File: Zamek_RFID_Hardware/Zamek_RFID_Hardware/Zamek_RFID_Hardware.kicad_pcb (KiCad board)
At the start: 2 copper layers, 53.6 x 61.5 mm, 30 parts, among them J1 Conn_01x08, J2 Conn_01x08, J3 Conn_01x04, J4 Conn_01x03, Q1 BC547

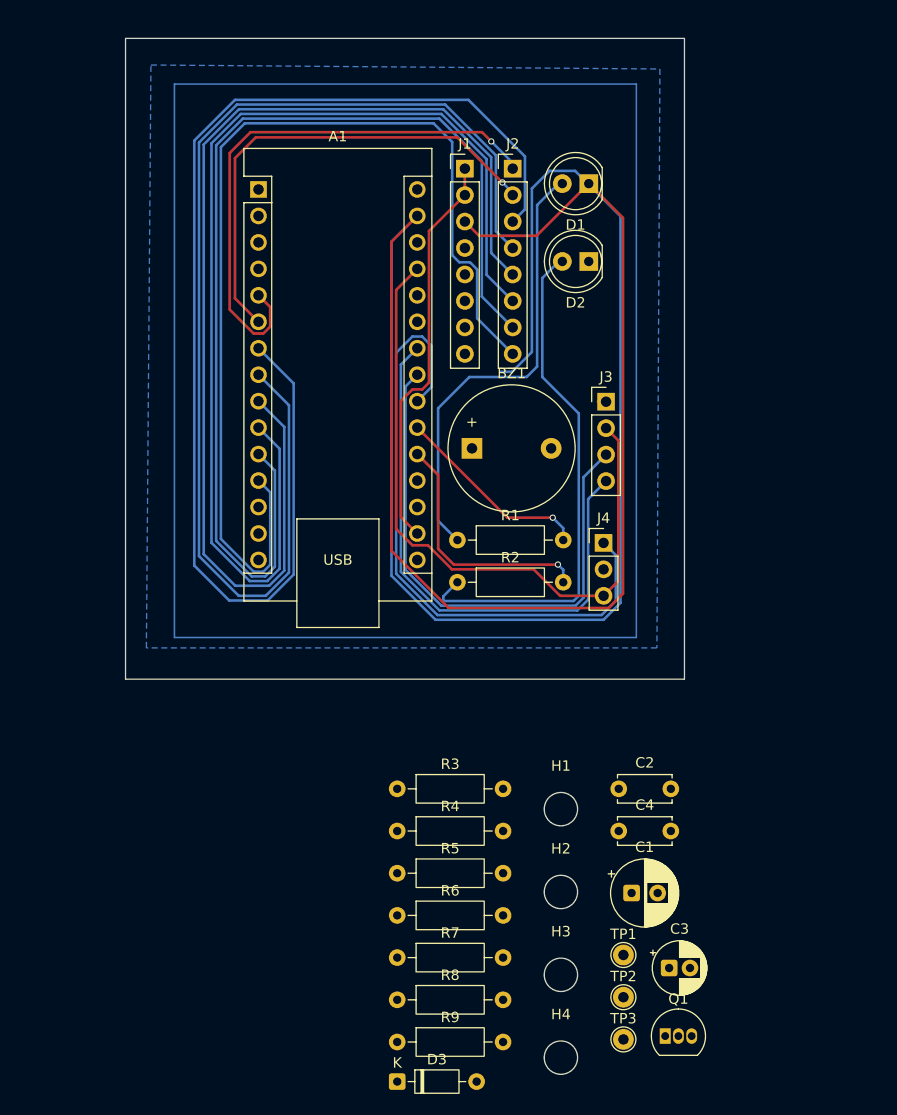
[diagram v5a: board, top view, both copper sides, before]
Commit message: docs: update pcb v1.1 progress notes
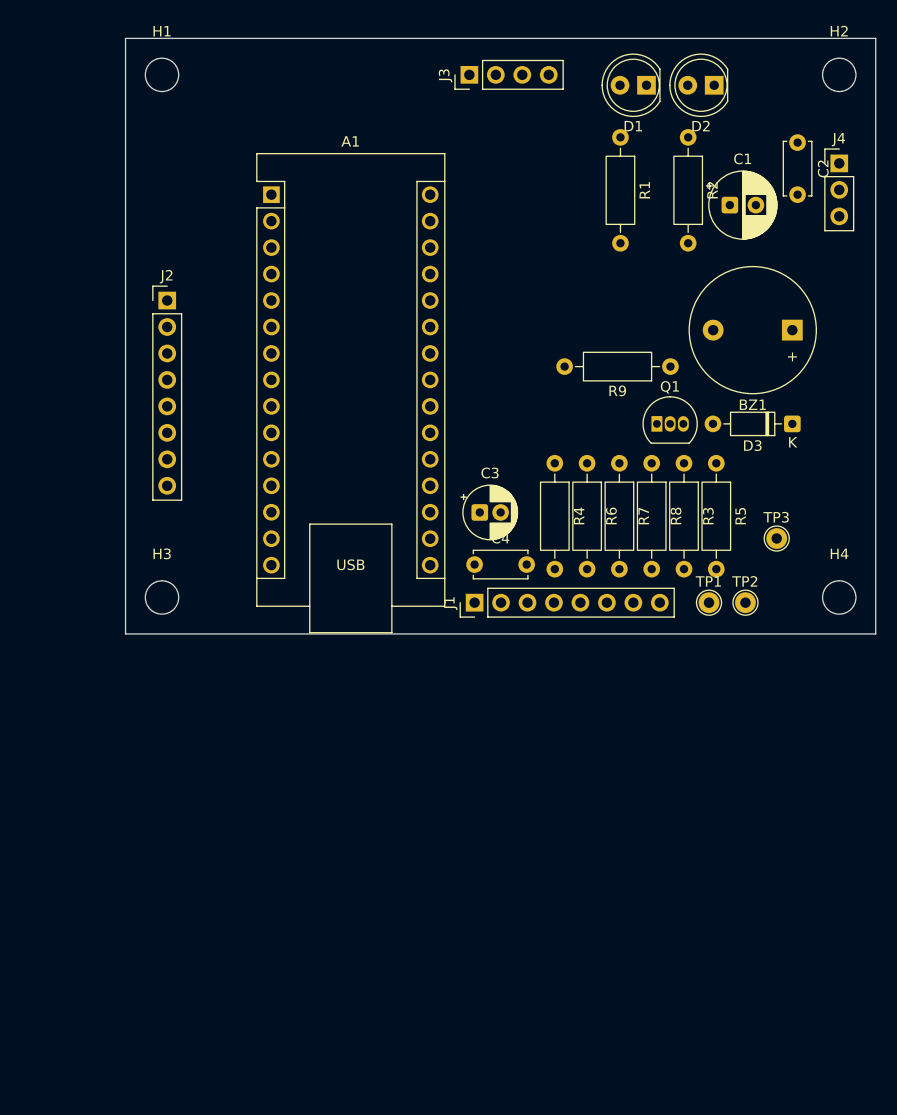
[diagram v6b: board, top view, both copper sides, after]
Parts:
- moved H2 82.9 mm to (178.5, 72.5)
- moved H1 80.2 mm to (113.5, 72.5)
- moved D3 73.6 mm to (174.0, 106.0), turned to 180 degrees
- moved R9 69.9 mm to (162.3, 100.5), turned to 180 degrees
- moved C1 66.7 mm to (168.0, 85.0)
- moved C2 64.4 mm to (174.5, 79.0), turned to -90 degrees
- moved Q1 58.8 mm to (161.0, 106.0)
- moved R8 57.0 mm to (160.5, 109.8), turned to -90 degrees
- moved H3 52.7 mm to (113.5, 122.7)
- moved R7 52.0 mm to (157.4, 109.8), turned to -90 degrees
- moved H4 51.6 mm to (178.5, 122.7)
- moved TP3 50.3 mm to (172.5, 117.0)
- moved R5 49.9 mm to (166.7, 109.8), turned to -90 degrees
- moved R2 48.1 mm to (164.0, 78.5), turned to -90 degrees
- moved C3 47.4 mm to (144.0, 114.5)
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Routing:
- net GND: track 241.8 -> 0.00 mm
- net /KEY_C2: track 118.2 -> 0.00 mm
- net /KEY_C1: track 112.6 -> 0.00 mm
- net /KEY_R1: track 109.2 -> 0.00 mm
- net /KEY_R2: track 105.3 -> 0.00 mm
- net /KEY_R3: track 102.3 -> 0.00 mm
- net /KEY_R4: track 99.7 -> 0.00 mm
- net +5V: track 65.5 -> 0.00 mm
- net /RELAY: track 60.8 -> 0.00 mm
- net /I2C_SCL: track 54.1 -> 0.00 mm
- net /KEY_C4: track 53.4 -> 0.00 mm, vias 1 -> 0
- net /I2C_SDA: track 52.6 -> 0.00 mm
- net Net-(D2-A): track 50.1 -> 0.00 mm
- net /KEY_C3: track 46.5 -> 0.00 mm, vias 1 -> 0
- net Net-(D1-A): track 43.3 -> 0.00 mm
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- removed copper zone on B.Cu, net GND
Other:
- board size 53.6 x 61.5 mm -> 72 x 57.2 mm

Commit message: F8 and the first tracks
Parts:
- moved R1 1.00 mm to (156.5, 78.5)
- moved D1 0.50 mm to (159.5, 73.5)
- moved D2 0.50 mm to (166.0, 73.5)
- turned Q1 to 180 degrees
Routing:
- net +5V: track 0.00 -> 119.2 mm
- net /RELAY: track 0.00 -> 61.9 mm
- net /LED_ZIELONA: track 0.00 -> 33.4 mm
- net /I2C_SDA: track 0.00 -> 32.9 mm
- net /I2C_SCL: track 0.00 -> 31.5 mm
- net /LED_CZERWONA: track 0.00 -> 25.3 mm
- net /BUZZER: track 0.00 -> 17.6 mm
- net Net-(BZ1--): track 0.00 -> 14.4 mm
- net /KEY_R4: track 0.00 -> 10.0 mm
- net /KEY_R3: track 0.00 -> 10.0 mm
- net /KEY_R2: track 0.00 -> 10.0 mm
- net /KEY_R1: track 0.00 -> 10.0 mm
- net /KEY_C4: track 0.00 -> 10.0 mm
- net /KEY_C3: track 0.00 -> 10.0 mm
- net /KEY_C2: track 0.00 -> 10.0 mm
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
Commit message: hw: route all signal and power nets
- Power on F.Cu with 0.6 mm tracks, decoupling caps placed in the current path
- Keypad: 8 straight parallel tracks
- Crossing nets (SDA, RELAY, LEDs, SCK, MISO) on B.Cu, no vias
- SPI routed under the Nano between header pins
- GND left for copper pour
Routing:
- net /RFID_SDA: track 0.00 -> 42.8 mm
- net +3.3V: track 0.00 -> 38.0 mm
- net /RFID_MISO: track 0.00 -> 31.2 mm
- net /RFID_MOSI: track 0.00 -> 30.2 mm
- net /RFID_SCK: track 0.00 -> 29.3 mm
- net /RFID_SDA_3V3: track 0.00 -> 10.1 mm
- net /RFID_MOSI_3V3: track 0.00 -> 7.11 mm
- net /RFID_SCK_3V3: track 0.00 -> 6.88 mm
